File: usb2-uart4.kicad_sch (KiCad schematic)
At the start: 14 parts, among them U1 FT4232H, U2 NUP2202, U3 93LCxxB, Y1 12.000 MHz

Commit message: Flush
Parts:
- added C10, C11, C12, C7, C8, C9: 3.3uF, Capacitor_SMD:C_0805_2012Metric_Pad1.18x1.45mm_HandSolder, symbol Device:C_Small
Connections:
- net GND: now also C10.1, C11.1, C12.1, C7.1, C8.1, C9.1
- net VIN 3.3V: now also C7.2, C8.2, C9.2
- net at C3.2, U1.12 (VCORE), U1.37 (VCORE)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: now also C10.2, C11.2, C12.2
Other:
- moved on the sheet: C3, C6

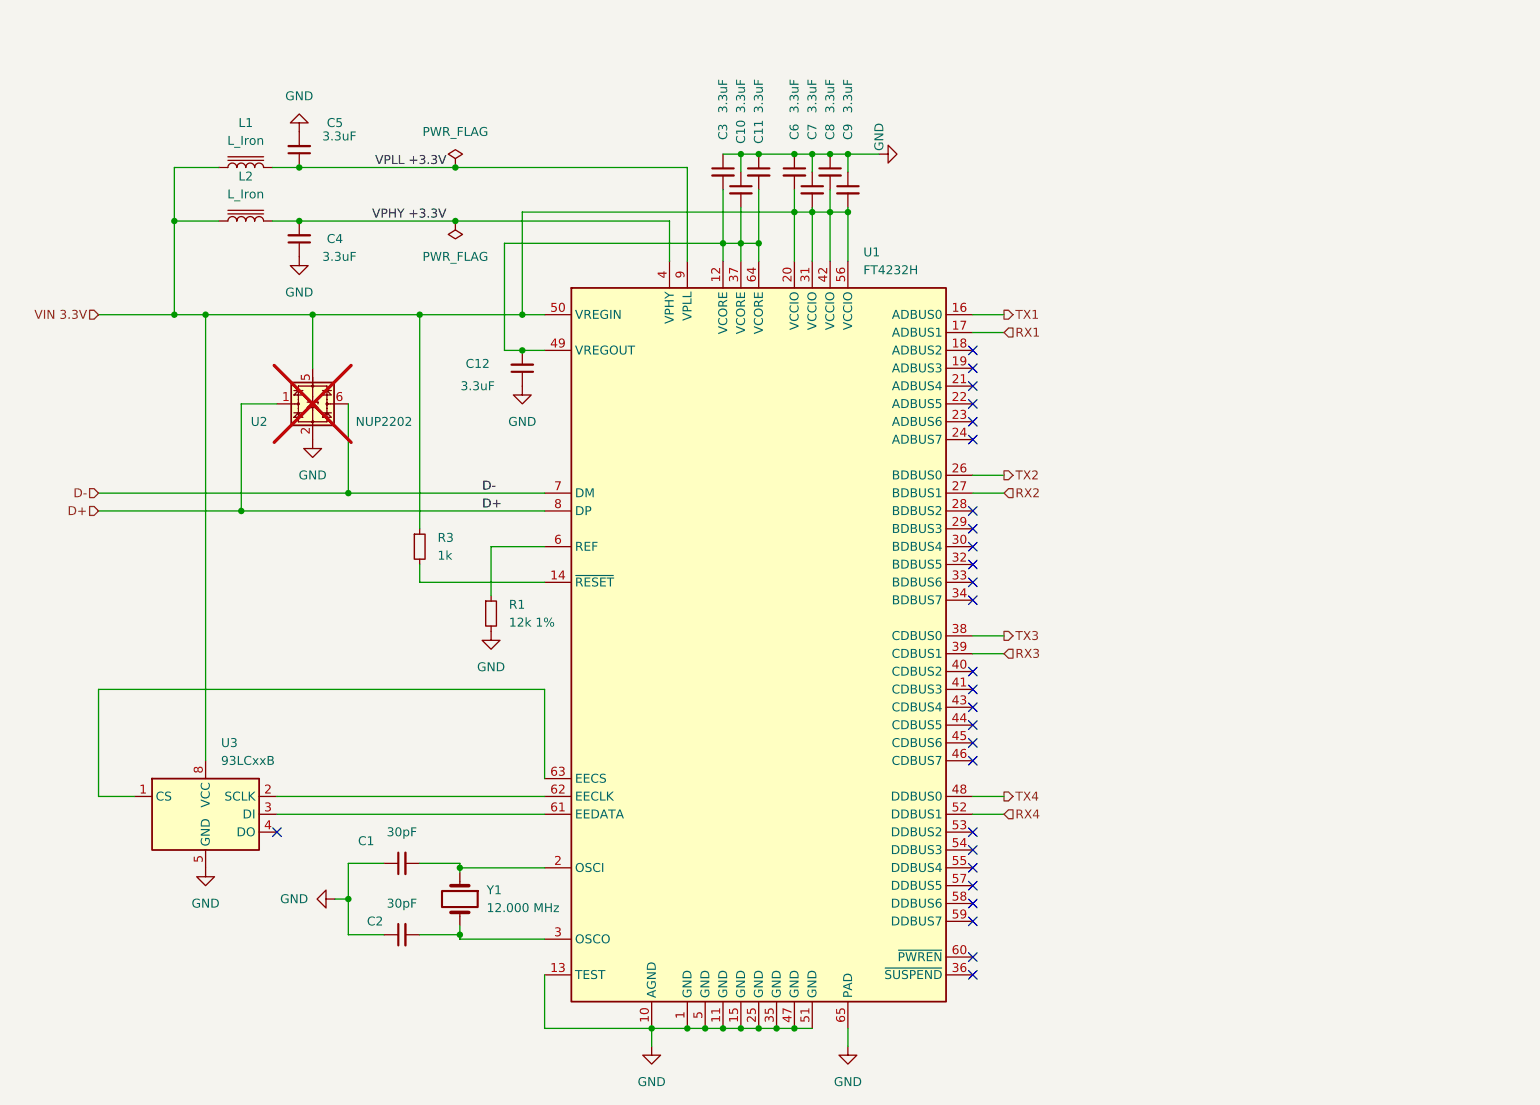
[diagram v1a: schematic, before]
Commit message: switch to CH344Q
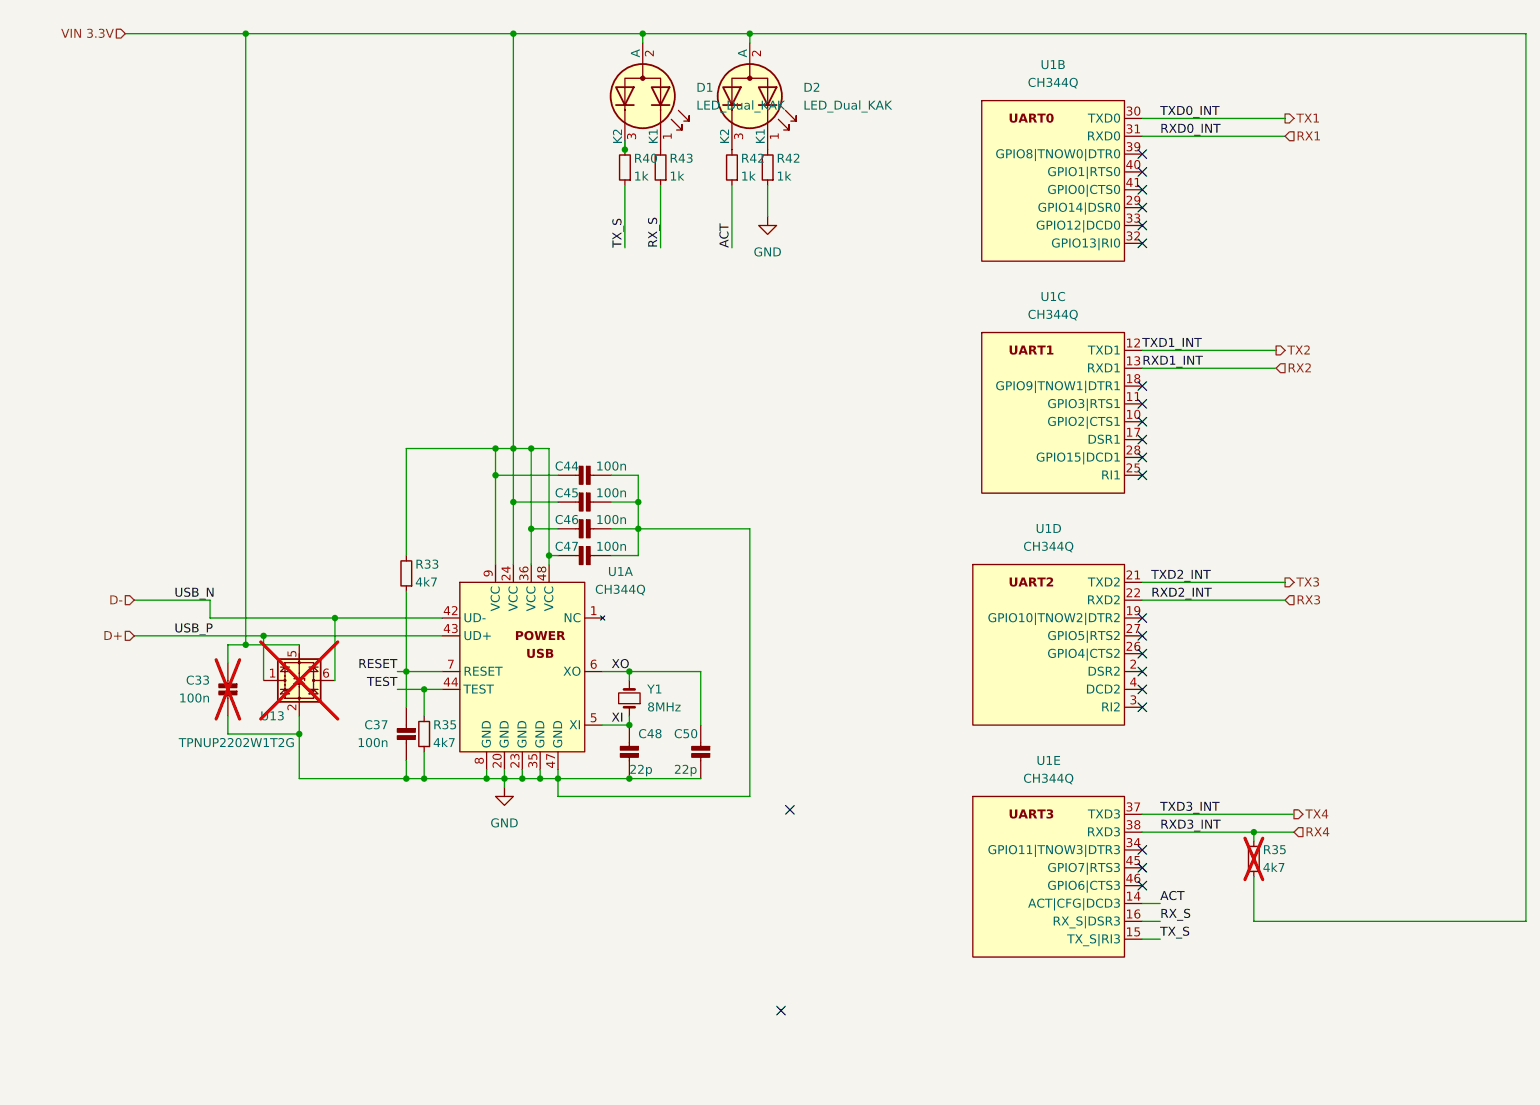
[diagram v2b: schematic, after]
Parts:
- removed C1, C2: 30pF, Capacitor_SMD:C_0805_2012Metric_Pad1.18x1.45mm_HandSolder, symbol Device:C_Small
- removed C10, C11, C12, C3, C4, C5, C6, C7, C8, C9: 3.3uF, Capacitor_SMD:C_0805_2012Metric_Pad1.18x1.45mm_HandSolder, symbol Device:C_Small
- removed L1, L2: L_Iron, Inductor_SMD:L_0805_2012Metric_Pad1.15x1.40mm_HandSolder, symbol Device:L_Iron
- removed R1: 12k 1%, Resistor_SMD:R_0805_2012Metric_Pad1.20x1.40mm_HandSolder, symbol Device:R_Small
- removed R3: 1k, Resistor_SMD:R_0805_2012Metric_Pad1.20x1.40mm_HandSolder, symbol Device:R_Small
- removed U1: FT4232H, Package_DFN_QFN:QFN-64-1EP_9x9mm_P0.5mm_EP6x6mm_ThermalVias, symbol Interface_USB:FT4232H
- removed U2: NUP2202, Package_TO_SOT_SMD:SOT-363_SC-70-6, symbol Power_Protection:NUP2202
- removed U3: 93LCxxB, Package_SO:SOIC-8_3.9x4.9mm_P1.27mm, symbol Memory_EEPROM:93LCxxB
- removed Y1: 12.000 MHz, Crystal:Crystal_HC49-U_Vertical, symbol Device:Crystal
- added C33, C37, C44, C45, C46, C47: 100n, Capacitor_SMD:C_0603_1608Metric_Pad1.08x0.95mm_HandSolder, symbol H_passives:CAP_NP
- added C48, C50: 22p, Capacitor_SMD:C_0805_2012Metric_Pad1.18x1.45mm_HandSolder, symbol H_passives:CAP_NP
- added D1, D2: LED_Dual_KAK, LED_THT:LED_D5.0mm-3, symbol Device:LED_Dual_KAK
- added R33, R35 (x2): 4k7, Resistor_SMD:R_0805_2012Metric_Pad1.20x1.40mm_HandSolder, symbol Device:R_Small
- added R40, R42 (x2), R43: 1k, Resistor_SMD:R_0805_2012Metric_Pad1.20x1.40mm_HandSolder, symbol Device:R_Small
- added U1: CH344Q, Package_QFP:LQFP-48_7x7mm_P0.5mm, symbol H_interface_esd:CH344Q
- added U13: TPNUP2202W1T2G, Package_TO_SOT_SMD:SOT-363_SC-70-6, symbol Power_Protection:NUP2202
- added Y1: 8MHz, Crystal:Crystal_HC49-U_Vertical, symbol Device:Crystal_Small
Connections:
- net D+: now also U1.43 (UD+), U13.1
- net D-: now also U1.42 (UD-), U13.6
- net GND: now also C33.1, C37.1, C44.1, C45.1, C46.1, C47.1, C48.1, C50.1, R35.1, R42.1, U1.20 (GND), U1.23 (GND), U1.35 (GND), U1.47 (GND), U1.8 (GND), U13.2
- net RX1: now also U1.31 (RXD0)
- net RX2: now also U1.13 (RXD1)
- net RX3: now also U1.22 (RXD2)
- net RX4: now also R35.2, U1.38 (RXD3)
- net TX1: now also U1.30 (TXD0)
- net TX2: now also U1.12 (TXD1)
- net TX3: now also U1.21 (TXD2)
- net TX4: now also U1.37 (TXD3)
- net VIN 3.3V: now also C33.2, C44.2, C45.2, C46.2, C47.2, D1.2 (A), D2.2 (A), R33.2, R35.1, U1.24 (VCC), U1.36 (VCC), U1.48 (VCC), U1.9 (VCC), U13.5
- new net: D1.1 (K1), R43.2
- new net: D1.3 (K2), R40.2
- new net: D2.1 (K1), R42.2
- new net: D2.3 (K2), R42.2
- new net ACT: R42.1, U1.14 (ACT|CFG|DCD3)
- new net RESET: C37.2, R33.1, U1.7 (RESET)
- new net RX_S: R43.1, U1.16 (RX_S|DSR3)
- new net TEST: R35.2, U1.44 (TEST)
- new net TX_S: R40.1, U1.15 (TX_S|RI3)
- new net XI: C48.2, U1.5 (XI), Y1.1
- new net XO: C50.2, U1.6 (XO), Y1.2
- no-connect marks 27 -> 23

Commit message: More feng shui
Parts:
- added C25: 4n7, Capacitor_SMD:C_0805_2012Metric_Pad1.18x1.45mm_HandSolder, symbol H_passives:CAP_NP
- added C47 (x2): 100n, Capacitor_SMD:C_0805_2012Metric_Pad1.18x1.45mm_HandSolder, symbol H_passives:CAP_NP
- added C48: 12p, Capacitor_SMD:C_0805_2012Metric_Pad1.18x1.45mm_HandSolder, symbol H_passives:CAP_NP
- added L1 (x2): L_Ferrite_Small, Inductor_SMD:L_TDK_NLV25_2.5x2.0mm, symbol Device:L_Ferrite_Small
- added R22: 1M, Resistor_SMD:R_0805_2012Metric_Pad1.20x1.40mm_HandSolder, symbol Device:R_Small
- added X1: ASV-xxxMHz, Oscillator:Oscillator_SMD_Abracon_ASV-4Pin_7.0x5.1mm, symbol Oscillator:ASV-xxxMHz
- C37: footprint Capacitor_SMD:C_0603_1608Metric_Pad1.08x0.95mm_HandSolder -> Capacitor_SMD:C_0805_2012Metric_Pad1.18x1.45mm_HandSolder
- C48, C50: now not fitted; now left out of the parts list
- U1: symbol H_interface_esd:CH344Q -> isouart4:CH344Q
- Y1: footprint Crystal:Crystal_HC49-U_Vertical -> Crystal:Crystal_SMD_7050-4Pin_7.0x5.0mm; now not fitted; now left out of the parts list
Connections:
- net VIN 3.3V: now also C47.1, L1.1, L1.2; no longer C44.2, C45.2, C46.2, C47.2, R33.2, U1.24 (VCC), U1.36 (VCC), U1.48 (VCC), U1.9 (VCC)
- net XI: now also C48.2, X1.3 (OUT)
- net GND renamed GNDUSBUART
- net GNDUSBUART: now also C25.1, C47.1, C47.2, C48.1, R22.1, X1.2 (GND)
- new net: C44.2, C45.2, C46.2, C47.2, L1.1, R33.2, U1.24 (VCC), U1.36 (VCC), U1.48 (VCC), U1.9 (VCC)
- new net: C47.2, L1.2, X1.1 (EN), X1.4 (Vdd)
- new net SHLDUSB: C25.2, R22.2
- no-connect marks 23 -> 21

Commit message: pcb-route all uart channels
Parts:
- C47, C48, L1, X1: now not fitted; now left out of the parts list
- C48, C50, Y1: now fitted; now in the parts list
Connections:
- net GNDUSBUART: now also Y1.2 (GND), Y1.4 (GND)
- net XO: now also Y1.3; no longer Y1.2
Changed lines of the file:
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@@
   (junction (at 135.89 18.415) (diameter 0) (color 0 0 0 0)
   )
+  (junction (at 130.175 124.46) (diameter 0) (color 0 0 0 0)
+  )
   (junction (at 117.475 71.12) (diameter 0) (color 0 0 0 0)
   )
@@
   (junction (at 79.375 105.41) (diameter 0) (color 0 0 0 0)
   )
+  (junction (at 137.795 124.46) (diameter 0) (color 0 0 0 0)
+  )
   (junction (at 86.995 118.11) (diameter 0) (color 0 0 0 0)
   )
@@
   (junction (at 81.915 104.14) (diameter 0) (color 0 0 0 0)
   )
-  (junction (at 130.81 134.62) (diameter 0) (color 0 0 0 0)
-  )
   (junction (at 153.67 120.015) (diameter 0) (color 0 0 0 0)
   )
+  (junction (at 131.445 116.84) (diameter 0) (color 0 0 0 0)
+  )
   (junction (at 222.885 132.08) (diameter 0) (color 0 0 0 0)
   )
@@
   (junction (at 135.255 88.9) (diameter 0) (color 0 0 0 0)
   )
+  (junction (at 131.445 134.62) (diameter 0) (color 0 0 0 0)
+  )
   (junction (at 117.475 85.09) (diameter 0) (color 0 0 0 0)
   )
@@
   )
   (junction (at 120.015 88.9) (diameter 0) (color 0 0 0 0)
-  )
-  (junction (at 130.81 116.84) (diameter 0) (color 0 0 0 0)
   )
   (junction (at 83.82 140.97) (diameter 0) (color 0 0 0 0)
@@
     (stroke (width 0) (type default))
   )
-  (wire (pts (xy 130.81 134.62) (xy 130.81 116.84))
+  (wire (pts (xy 131.445 134.62) (xy 131.445 116.84))
     (stroke (width 0) (type default))
   )
@@
     (stroke (width 0) (type default))
   )
+  (wire (pts (xy 137.795 124.46) (xy 144.145 124.46))
+    (stroke (width 0) (type default))
+  )
   (wire (pts (xy 207.01 33.02) (xy 227.33 33.02))
     (stroke (width 0) (type default))
@@
     (stroke (width 0) (type default))
   )
+  (wire (pts (xy 130.175 113.03) (xy 130.175 124.46))
+    (stroke (width 0) (type default))
+  )
   (wire (pts (xy 153.67 123.19) (xy 153.67 120.015))
     (stroke (width 0) (type default))
@@
     (stroke (width 0) (type default))
   )
-  (wire (pts (xy 123.825 124.46) (xy 133.985 124.46))
+  (wire (pts (xy 123.825 124.46) (xy 130.175 124.46))
     (stroke (width 0) (type default))
   )
@@
     (stroke (width 0) (type default))
   )
-  (wire (pts (xy 130.81 116.84) (xy 133.985 116.84))
+  (wire (pts (xy 130.175 116.84) (xy 131.445 116.84))
     (stroke (width 0) (type default))
   )
@@
     (stroke (width 0) (type default))
   )
-  (wire (pts (xy 146.05 134.62) (xy 130.81 134.62))
+  (wire (pts (xy 146.05 134.62) (xy 131.445 134.62))
     (stroke (width 0) (type default))
   )
@@
     (stroke (width 0) (type default))
   )
+  (wire (pts (xy 130.175 124.46) (xy 133.985 124.46))
+    (stroke (width 0) (type default))
+  )
   (wire (pts (xy 123.825 81.28) (xy 114.935 81.28))
     (stroke (width 0) (type default))
@@
     (stroke (width 0) (type default))
   )
+  (wire (pts (xy 137.795 113.03) (xy 137.795 124.46))
+    (stroke (width 0) (type default))
+  )
   (wire (pts (xy 123.825 127) (xy 123.825 124.46))
     (stroke (width 0) (type default))
@@
     (stroke (width 0) (type default))
   )
-  (wire (pts (xy 130.175 116.84) (xy 130.81 116.84))
-    (stroke (width 0) (type default))
-  )
   (wire (pts (xy 117.475 71.12) (xy 117.475 71.755))
     (stroke (width 0) (type default))
@@
     (stroke (width 0) (type default))
   )
+  (wire (pts (xy 131.445 116.84) (xy 133.985 116.84))
+    (stroke (width 0) (type default))
+  )
   (wire (pts (xy 135.255 88.9) (xy 135.255 85.09))
     (stroke (width 0) (type default))
@@
     (stroke (width 0) (type default))
   )
-  (wire (pts (xy 133.985 124.46) (xy 144.145 124.46))
+  (wire (pts (xy 133.985 124.46) (xy 137.795 124.46))
     (stroke (width 0) (type default))
   )
@@
   )
   (wire (pts (xy 131.445 92.71) (xy 135.255 92.71))
+    (stroke (width 0) (type default))
+  )
+  (wire (pts (xy 131.445 134.62) (xy 130.81 134.62))
     (stroke (width 0) (type default))
   )
@@
   )
   (symbol (lib_id "Device:L_Ferrite_Small") (at 139.7 71.12 90) (unit 1)
-    (in_bom yes) (on_board yes) (dnp no) (fields_autoplaced)
+    (in_bom no) (on_board no) (dnp yes) (fields_autoplaced)
     (property "Reference" "L1" (at 139.7 64.77 90)
       (effects (font (size 1.27 1.27)))
@@
     )
     (property "Datasheet" "~" (at 139.7 71.12 0)
+      (effects (font (size 1.27 1.27)) hide)
+    )
+    (property "Sim.Enable" "0" (at 139.7 71.12 0)
       (effects (font (size 1.27 1.27)) hide)
     )
@@
   )
   (symbol (lib_id "Device:Crystal_Small") (at 133.985 113.03 90) (unit 1)
-    (in_bom no) (on_board no) (dnp yes) (fields_autoplaced)
-    (property "Reference" "Y1" (at 136.525 111.7599 90)
-      (effects (font (size 1.27 1.27)) (justify right))
-    )
-    (property "Value" "8MHz" (at 136.525 114.2999 90)
-      (effects (font (size 1.27 1.27)) (justify right))
-    )
-    (property "Footprint" "Crystal:Crystal_SMD_7050-4Pin_7.0x5.0mm" (at 133.985 113.03 0)
+    (in_bom yes) (on_board yes) (dnp no)
+    (property "Reference" "Y1" (at 132.08 120.015 0)
+      (effects (font (size 1.27 1.27)) (justify right))
+    )
+    (property "Value" "8MHz" (at 129.54 119.38 0)
+      (effects (font (size 1.27 1.27)) (justify right))
+    )
+    (property "Footprint" "Crystal:Crystal_SMD_7050-4Pin_7.0x5.0mm" (at 120.015 110.49 0)
       (effects (font (size 1.27 1.27)) hide)
     )
@@
       (effects (font (size 1.27 1.27)) hide)
     )
-    (property "Sim.Enable" "0" (at 133.985 113.03 0)
-      (effects (font (size 1.27 1.27)) hide)
-    )
-    (pin "1")
-    (pin "2")
+    (pin "1")
+    (pin "2")
+    (pin "3")
+    (pin "4")
     (instances
       (project "4WD_UART"
@@
   )
   (symbol (lib_id "H_passives:CAP_NP") (at 158.75 120.015 270) (unit 1)
-    (in_bom yes) (on_board yes) (dnp no)
+    (in_bom no) (on_board no) (dnp yes)
     (property "Reference" "C47" (at 156.21 118.745 90)
       (effects (font (size 1.27 1.27)))
@@
       (effects (font (size 1.27 1.27)) hide)
     )
+    (property "Sim.Enable" "0" (at 158.75 120.015 0)
+      (effects (font (size 1.27 1.27)) hide)
+    )
     (pin "1")
     (pin "2")
@@
   )
   (symbol (lib_id "H_passives:CAP_NP") (at 130.81 138.43 180) (unit 1)
-    (in_bom yes) (on_board yes) (dnp no)
+    (in_bom no) (on_board no) (dnp yes)
     (property "Reference" "C48" (at 132.08 135.89 0)
       (effects (font (size 1.27 1.27)) (justify right))
@@
     )
     (property "Datasheet" "" (at 130.81 137.16 0)
+      (effects (font (size 1.27 1.27)) hide)
+    )
+    (property "Sim.Enable" "0" (at 130.81 138.43 0)
       (effects (font (size 1.27 1.27)) hide)
     )
@@
   )
   (symbol (lib_id "H_passives:CAP_NP") (at 144.145 120.65 180) (unit 1)
-    (in_bom no) (on_board no) (dnp yes)
+    (in_bom yes) (on_board yes) (dnp no)
     (property "Reference" "C50" (at 140.335 118.11 0)
       (effects (font (size 1.27 1.27)) (justify right))
@@
     )
     (property "Datasheet" "" (at 144.145 119.38 0)
-      (effects (font (size 1.27 1.27)) hide)
-    )
-    (property "Sim.Enable" "0" (at 144.145 120.65 0)
       (effects (font (size 1.27 1.27)) hide)
     )
@@
   )
   (symbol (lib_id "Oscillator:ASV-xxxMHz") (at 153.67 134.62 0) (mirror y) (unit 1)
-    (in_bom yes) (on_board yes) (dnp no)
+    (in_bom no) (on_board no) (dnp yes)
     (property "Reference" "X1" (at 140.97 130.9721 0)
       (effects (font (size 1.27 1.27)))
@@
     )
     (property "Datasheet" "http://www.abracon.com/Oscillators/ASV.pdf" (at 156.21 134.62 0)
+      (effects (font (size 1.27 1.27)) hide)
+    )
+    (property "Sim.Enable" "0" (at 153.67 134.62 0)
       (effects (font (size 1.27 1.27)) hide)
     )
@@
   )
   (symbol (lib_id "H_passives:CAP_NP") (at 133.985 120.65 180) (unit 1)
-    (in_bom no) (on_board no) (dnp yes)
+    (in_bom yes) (on_board yes) (dnp no)
     (property "Reference" "C48" (at 135.255 118.11 0)
       (effects (font (size 1.27 1.27)) (justify right))
@@
       (effects (font (size 1.27 1.27)) hide)
     )
-    (property "Sim.Enable" "0" (at 133.985 120.65 0)
-      (effects (font (size 1.27 1.27)) hide)
-    )
